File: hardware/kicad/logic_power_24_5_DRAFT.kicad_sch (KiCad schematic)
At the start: 19 parts, among them U101 LM5013DDAR

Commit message: chore: consolidate current CAD project
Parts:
- D101: footprint (none) -> Package_TO_SOT_SMD:TO-252-2
- U101: footprint Sirokko_Power:DDA0008B_LM5013DDAR_TI4214849B -> Sirokko_Power:DDA0008B_LM5013DDAR_TI4214849B_3D; MPN (none) -> LM5013DDAR
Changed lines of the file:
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@@
 		)
 	)
-	(property "Footprint" "Sirokko_Power:DDA0008B_LM5013DDAR_TI4214849B"
+	(property "Footprint" "Sirokko_Power:DDA0008B_LM5013DDAR_TI4214849B_3D"
 		(at 90.17 66.04 0)
 		(effects
@@
 		)
 	)
+	(property "MPN" "LM5013DDAR"
+	(id 0)
+	(at 90.17 66.04 0)
+	(effects
+		(font
+			(size 1.27 1.27)
+		)
+		(hide yes)
+	)
+)
 	(pin "1"
 )
@@
 		)
 	)
-	(property "Footprint" ""
+	(property "Footprint" "Package_TO_SOT_SMD:TO-252-2"
 		(at 119.38 86.36 0)
 		(effects

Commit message: hardware: verify WD_OK and close two GND gaps
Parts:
- C105, C106: value 47uF 16V X7R -> 47uF 16V X5R
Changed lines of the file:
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@@
 		)
 	)
-	(property "Value" "47uF 16V X7R"
+	(property "Value" "47uF 16V X5R"
 		(at 165.1 67.31 0)
 		(effects
@@
 		)
 	)
-	(property "Value" "47uF 16V X7R"
+	(property "Value" "47uF 16V X5R"
 		(at 185.42 67.31 0)
 		(effects

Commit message: WIP: publish current unfinished CAD sources
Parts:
- C103: value 22uF 100V BULK -> 100uF 100V EEU-FR2A101; footprint Capacitor_SMD:C_1210_3225Metric -> Sirokko_Power:CP_Radial_D10.0mm_P5.00mm_Courtyard_D11.0mm; MPN GRM32ER72A226KE20L -> EEU-FR2A101; Manufacturer (none) -> Panasonic Industry
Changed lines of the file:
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@@
 		)
 	)
-	(property "Value" "22uF 100V BULK"
+	(property "Value" "100uF 100V EEU-FR2A101"
 		(at 40.64 80.01 0)
 		(effects
@@
 		)
 	)
-	(property "Footprint" "Capacitor_SMD:C_1210_3225Metric"
+	(property "Footprint" "Sirokko_Power:CP_Radial_D10.0mm_P5.00mm_Courtyard_D11.0mm"
 		(at 40.64 76.2 0)
 		(effects
@@
 		)
 	)
-	(property "MPN" "GRM32ER72A226KE20L"
+	(property "MPN" "EEU-FR2A101"
 	(id 0)
 	(at 40.64 76.2 0)
 	(effects
+		(font
+			(size 1.27 1.27)
+		)
+		(hide yes)
+	)
+)
+	(property "Manufacturer" "Panasonic Industry"
+	(id 1)
+	(at 40.64 76.2 0)
+	(effects

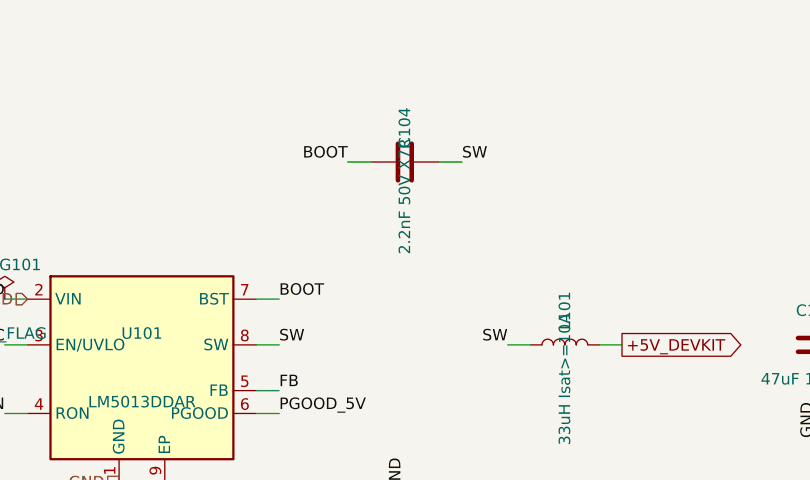
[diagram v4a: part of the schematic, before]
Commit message: Publish C104 C0G manufacturing draft
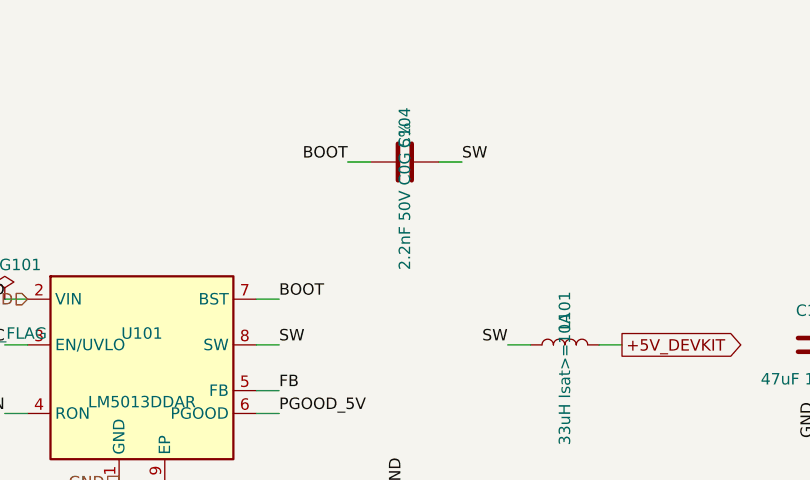
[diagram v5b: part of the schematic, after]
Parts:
- C104: value 2.2nF 50V X7R -> 2.2nF 50V C0G 5%; MPN CC0603KRX7R9BB222 -> GRM1885C1H222JA01D; Manufacturer (none) -> Murata
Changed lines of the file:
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@@
 			)
 		)
-		(property "Value" "2.2nF 50V X7R"
+		(property "Value" "2.2nF 50V C0G 5%"
 			(at 119.38 46.99 0)
 			(show_name no)
@@
 			)
 		)
-		(property "Datasheet" ""
+		(property "Datasheet" "https://pim.murata.com/asset/pim4/ceramicCapacitorSMD/GRM1885C1H222JA01-01A-EN_PDF_CERAMICCAPACITORSMD?lastModifiedDatetime=20260730162352"
 			(at 119.38 43.18 0)
 			(hide yes)
@@
 			)
 		)
-		(property "MPN" "CC0603KRX7R9BB222"
+		(property "MPN" "GRM1885C1H222JA01D"
 			(at 119.38 43.18 0)
 			(hide yes)
@@
 			)
 		)
+		(property "Manufacturer" "Murata"
+	(id 0)
+	(at 119.38 43.18 0)
+	(effects
+		(font
+			(size 1.27 1.27)
+		)
+		(hide yes)
+	)
+)
 		(pin "1"
 		)
